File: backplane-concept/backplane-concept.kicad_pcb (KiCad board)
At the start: 2 copper layers, 90 x 150 mm, 55 parts, among them J1 6473427-1, J2 PCIE_8x_Labeled, J3 PCIE_8x_Labeled, J4 PCIE_8x_Labeled, J5 CONN_MINI, J6 CONN_MINI, J7 CONN_MINI, J8 CONN_MINI, U1 PRIMARY, U2 SECONDARY, U3 NAU7802SGI, U4 ATA6561-GBQW-N, U5 ESP32-PICO-D4, U6 5V Reg, U7 AMS1117CD-5.0, U8 3.3V Reg, U9 AMS1117CD-3.3

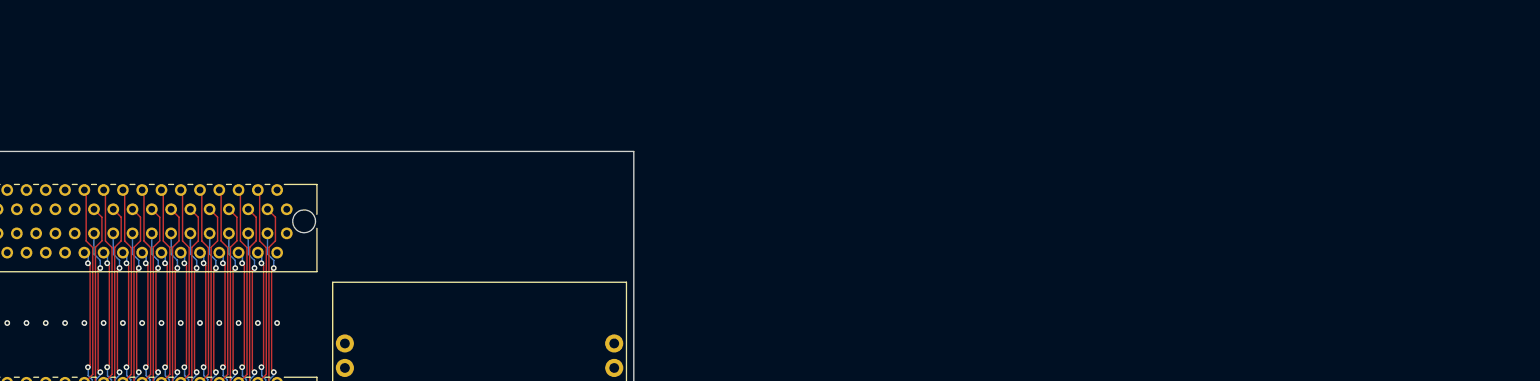
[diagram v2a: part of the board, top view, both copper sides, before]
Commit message: Add testpoints
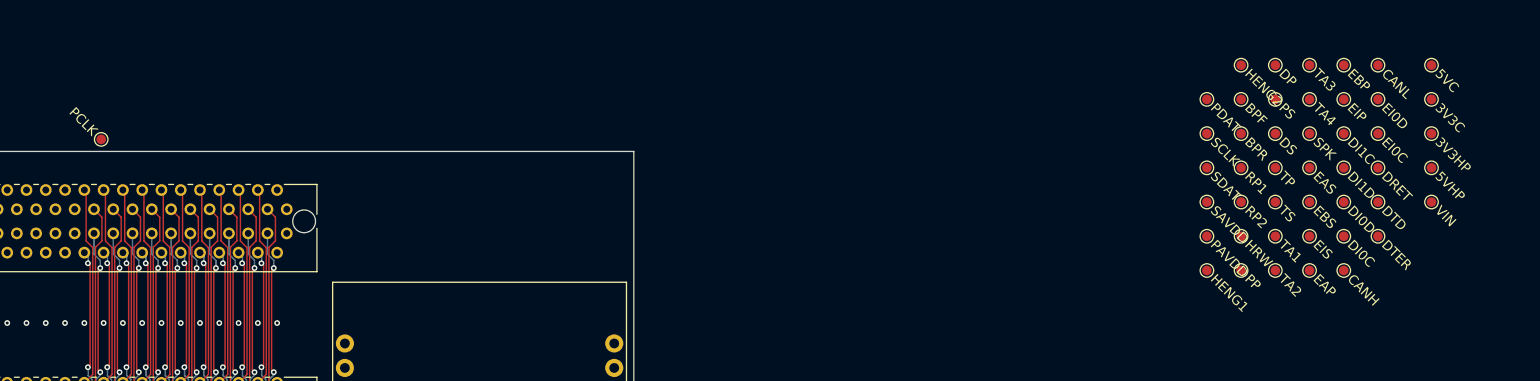
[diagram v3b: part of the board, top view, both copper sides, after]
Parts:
- added TP1: PCLK, !footprints:TestPoint_Pad_D1.0mm, F.Cu at (90.8, 32.8)
- added TP10: 5VHP, !footprints:TestPoint_Pad_D1.0mm, F.Cu at (228.8, 35.7)
- added TP11: VIN, !footprints:TestPoint_Pad_D1.0mm, F.Cu at (228.8, 39.2)
- added TP12: HENG1, !footprints:TestPoint_Pad_D1.0mm, F.Cu at (205.4, 46.4)
- added TP13: HENG2, !footprints:TestPoint_Pad_D1.0mm, F.Cu at (209.0, 25.1)
- added TP14: BPF, !footprints:TestPoint_Pad_D1.0mm, F.Cu at (209.0, 28.6)
- added TP15: BPR, !footprints:TestPoint_Pad_D1.0mm, F.Cu at (209.0, 32.1)
- added TP16: RP1, !footprints:TestPoint_Pad_D1.0mm, F.Cu at (209.0, 35.7)
- added TP17: RP2, !footprints:TestPoint_Pad_D1.0mm, F.Cu at (209.0, 39.2)
- added TP18: HRW, !footprints:TestPoint_Pad_D1.0mm, F.Cu at (209.0, 42.8)
- added TP19: PP, !footprints:TestPoint_Pad_D1.0mm, F.Cu at (209.0, 46.4)
- added TP2: PDAT, !footprints:TestPoint_Pad_D1.0mm, F.Cu at (205.4, 28.6)
- added TP20: DP, !footprints:TestPoint_Pad_D1.0mm, F.Cu at (212.6, 25.1)
- added TP21: PS, !footprints:TestPoint_Pad_D1.0mm, F.Cu at (212.6, 28.6)
- added TP22: DS, !footprints:TestPoint_Pad_D1.0mm, F.Cu at (212.6, 32.1)
- added TP23: TP, !footprints:TestPoint_Pad_D1.0mm, F.Cu at (212.6, 35.7)
- added TP24: TS, !footprints:TestPoint_Pad_D1.0mm, F.Cu at (212.6, 39.2)
- added TP25: TA1, !footprints:TestPoint_Pad_D1.0mm, F.Cu at (212.6, 42.8)
- added TP26: TA2, !footprints:TestPoint_Pad_D1.0mm, F.Cu at (212.6, 46.4)
- added TP27: TA3, !footprints:TestPoint_Pad_D1.0mm, F.Cu at (216.1, 25.1)
- added TP28: TA4, !footprints:TestPoint_Pad_D1.0mm, F.Cu at (216.1, 28.6)
- added TP29: SPK, !footprints:TestPoint_Pad_D1.0mm, F.Cu at (216.1, 32.1)
- added TP3: SCLK, !footprints:TestPoint_Pad_D1.0mm, F.Cu at (205.4, 32.1)
- added TP30: EAS, !footprints:TestPoint_Pad_D1.0mm, F.Cu at (216.1, 35.7)
- added TP31: EBS, !footprints:TestPoint_Pad_D1.0mm, F.Cu at (216.1, 39.2)
- added TP32: EIS, !footprints:TestPoint_Pad_D1.0mm, F.Cu at (216.1, 42.8)
- added TP33: EAP, !footprints:TestPoint_Pad_D1.0mm, F.Cu at (216.1, 46.4)
- added TP34: EBP, !footprints:TestPoint_Pad_D1.0mm, F.Cu at (219.7, 25.1)
- added TP35: EIP, !footprints:TestPoint_Pad_D1.0mm, F.Cu at (219.7, 28.6)
- added TP36: DI1C, !footprints:TestPoint_Pad_D1.0mm, F.Cu at (219.7, 32.1)
- added TP37: DI1D, !footprints:TestPoint_Pad_D1.0mm, F.Cu at (219.7, 35.7)
- added TP38: DI0D, !footprints:TestPoint_Pad_D1.0mm, F.Cu at (219.7, 39.2)
- added TP39: DI0C, !footprints:TestPoint_Pad_D1.0mm, F.Cu at (219.7, 42.8)
- added TP4: SDAT, !footprints:TestPoint_Pad_D1.0mm, F.Cu at (205.4, 35.7)
- added TP40: CANH, !footprints:TestPoint_Pad_D1.0mm, F.Cu at (219.7, 46.4)
- added TP41: CANL, !footprints:TestPoint_Pad_D1.0mm, F.Cu at (223.2, 25.1)
- added TP42: EI0D, !footprints:TestPoint_Pad_D1.0mm, F.Cu at (223.2, 28.6)
- added TP43: EI0C, !footprints:TestPoint_Pad_D1.0mm, F.Cu at (223.2, 32.1)
- added TP44: DRET, !footprints:TestPoint_Pad_D1.0mm, F.Cu at (223.2, 35.7)
- added TP45: DTD, !footprints:TestPoint_Pad_D1.0mm, F.Cu at (223.2, 39.2)
- added TP46: DTER, !footprints:TestPoint_Pad_D1.0mm, F.Cu at (223.2, 42.8)
- added TP5: SAVDD, !footprints:TestPoint_Pad_D1.0mm, F.Cu at (205.4, 39.2)
- added TP6: PAVDD, !footprints:TestPoint_Pad_D1.0mm, F.Cu at (205.4, 42.8)
- added TP7: 5VC, !footprints:TestPoint_Pad_D1.0mm, F.Cu at (228.8, 25.1)
- added TP8: 3V3C, !footprints:TestPoint_Pad_D1.0mm, F.Cu at (228.8, 28.6)
- added TP9: 3V3HP, !footprints:TestPoint_Pad_D1.0mm, F.Cu at (228.8, 32.1)
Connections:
- net AVDD_S renamed AVDD_P
- C10 pad 1: +3.3VA -> /PSU/3V3_CLEAN
- C12 pad 1: +8V -> /PSU/VIN
- C14 pad 1: +5V -> /PSU/5V_HP
- C15 pad 1: +5V -> /PSU/5V_HP
- C18 pad 1: +8V -> /PSU/VIN
- C23 pad 1: +3V3 -> /PSU/3V3_HP
- C24 pad 1: +3V3 -> /PSU/3V3_HP
- C25 pad 1: +8V -> /PSU/VIN
- C26 pad 1: +8V -> /PSU/VIN
- C7 pad 1: +8V -> /PSU/VIN
- C8 pad 1: +5VA -> /PSU/5V_CLEAN
- C9 pad 1: +8V -> /PSU/VIN
- L1 pad 2: +5V -> /PSU/5V_HP
- L2 pad 2: +3V3 -> /PSU/3V3_HP
- R6 pad 1: +5V -> /PSU/5V_HP
- R9 pad 1: +3V3 -> /PSU/3V3_HP
- U2 pad 7: LOADC_CLK_P -> LOADC_CLK_S
- U6 pad 2: +8V -> /PSU/VIN
- U6 pad 3: +8V -> /PSU/VIN
- U7 pad 2: +5VA -> /PSU/5V_CLEAN
- U7 pad 3: +8V -> /PSU/VIN
- U8 pad 2: +8V -> /PSU/VIN
- U8 pad 3: +8V -> /PSU/VIN
- U9 pad 2: +3.3VA -> /PSU/3V3_CLEAN
- U9 pad 3: +8V -> /PSU/VIN
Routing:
- net /PSU/VIN: vias 0 -> 4
- net +8V: vias 26 -> 22

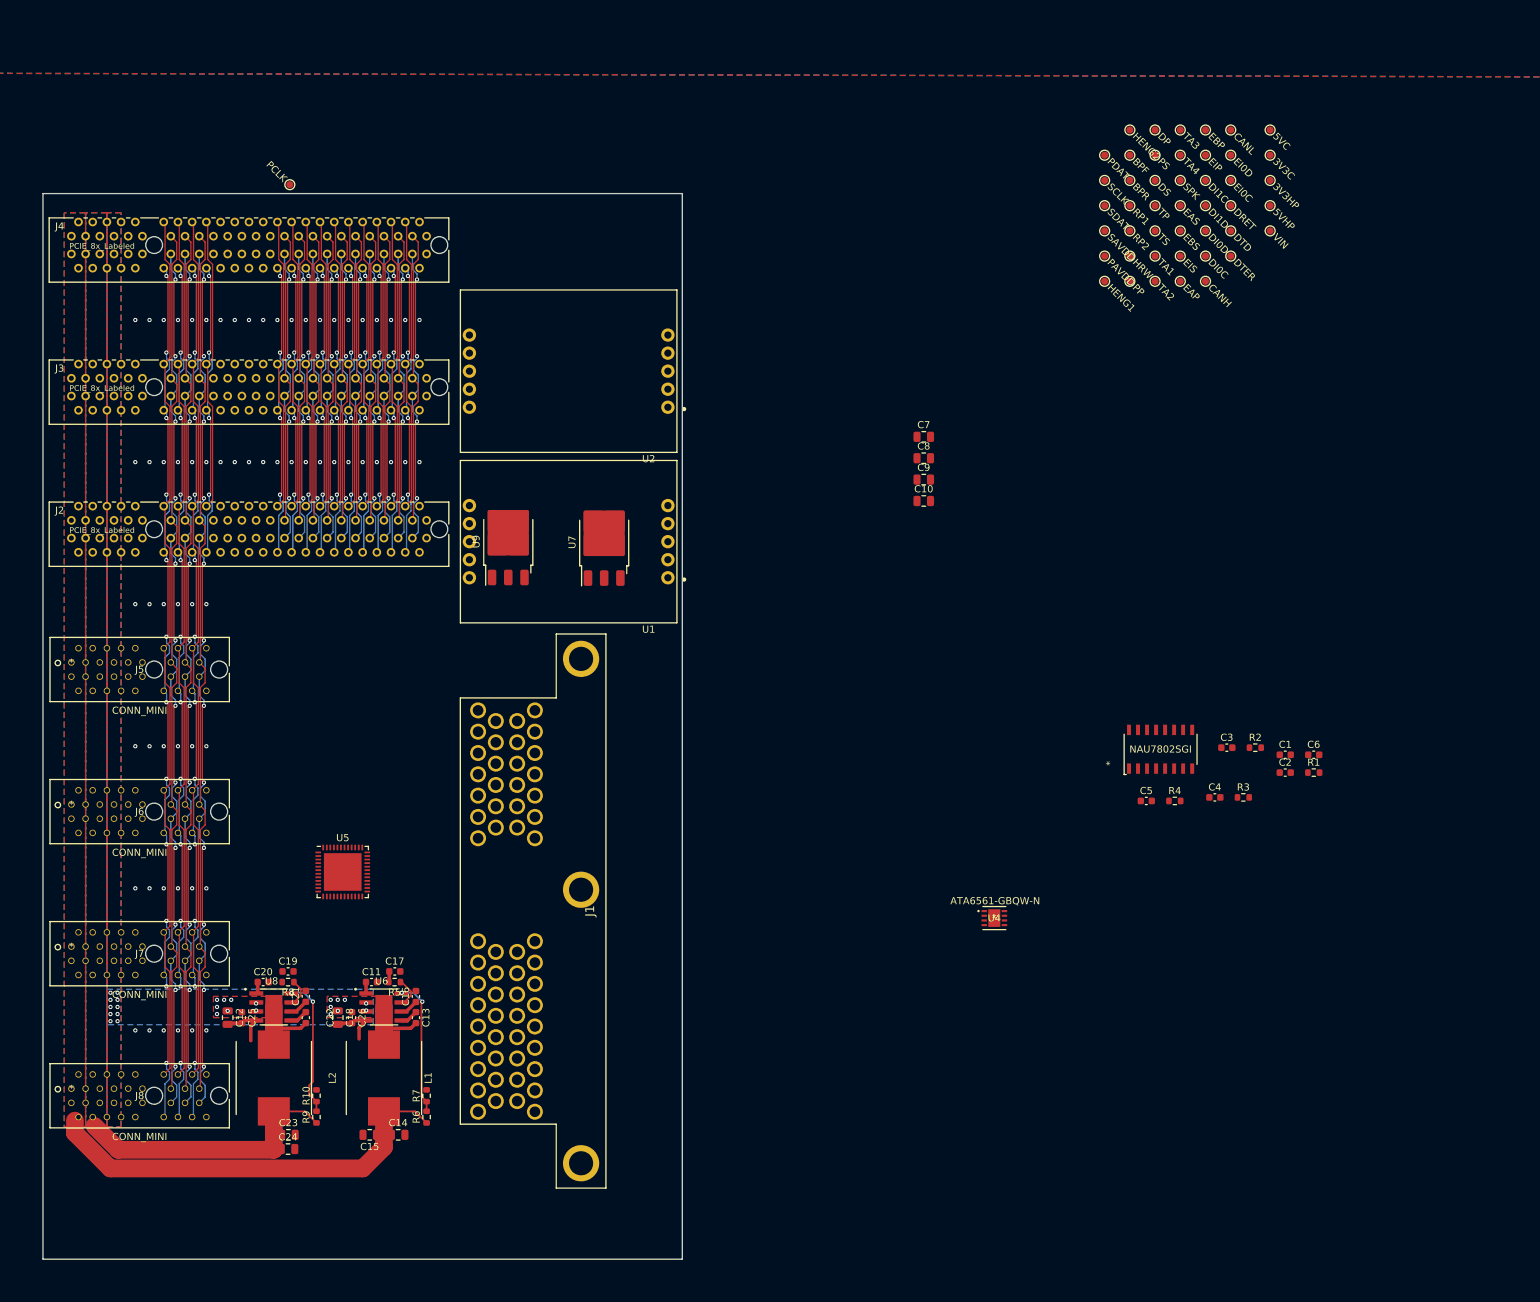
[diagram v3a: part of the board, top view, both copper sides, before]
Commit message: Route some test points
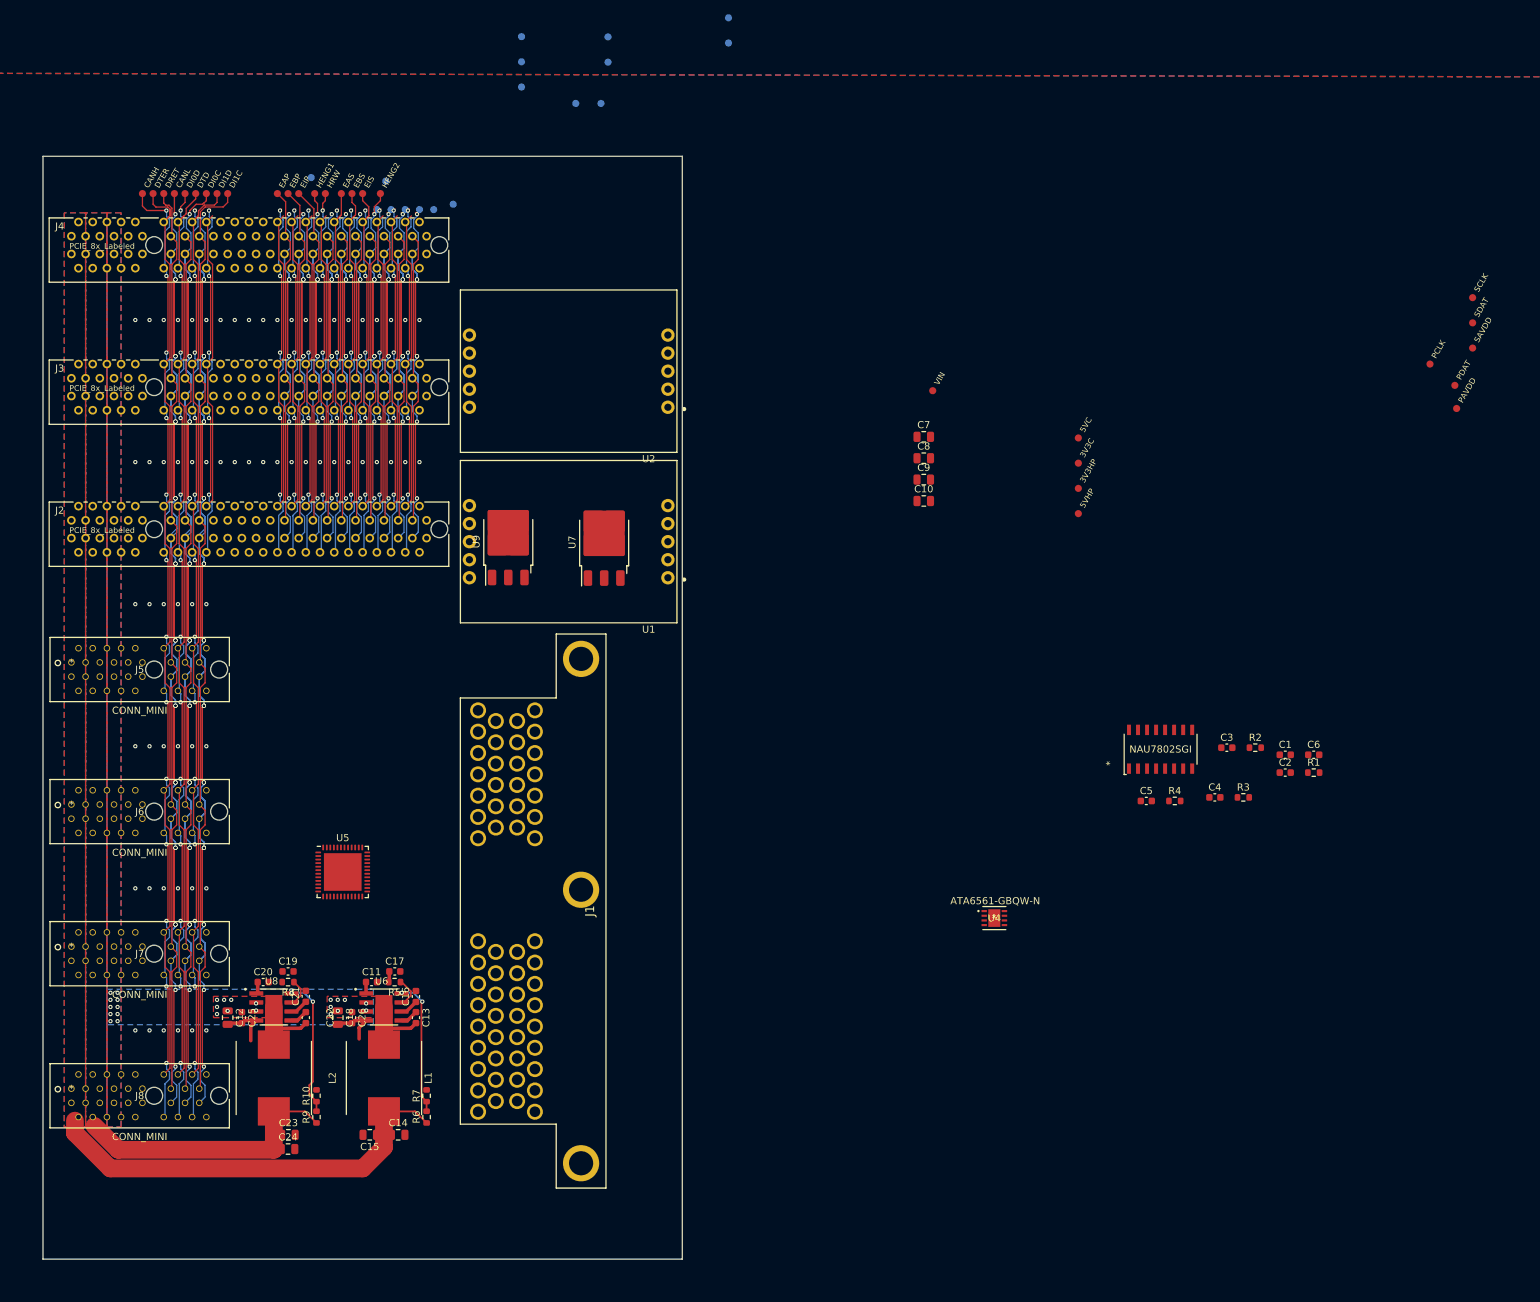
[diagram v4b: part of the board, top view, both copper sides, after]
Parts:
- TP14, TP15, TP16, TP17, TP19, TP20, TP21, TP22, TP23, TP24, TP25, TP26, TP27, TP28, TP29, TP42, TP43: moved to B.Cu
- moved TP1 162.5 mm to (251.2, 58.0), turned to 0 degrees
- moved TP46 152.0 mm to (71.5, 34.0)
- moved TP44 150.2 mm to (73.0, 34.0)
- moved TP40 150.2 mm to (70.0, 34.0)
- moved TP41 149.0 mm to (74.5, 34.0)
- moved TP45 145.8 mm to (77.5, 34.0)
- moved TP38 143.7 mm to (76.0, 34.0)
- moved TP39 140.9 mm to (79.0, 34.0)
- moved TP37 139.2 mm to (80.5, 34.0)
- moved TP36 137.7 mm to (82.0, 34.0)
- moved TP34 129.5 mm to (90.5, 34.0)
- moved TP35 127.8 mm to (92.0, 34.0)
- moved TP33 127.7 mm to (89.0, 34.0)
- moved TP30 118.1 mm to (98.0, 34.0)
- moved TP31 116.7 mm to (99.5, 34.0)
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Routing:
- net I2C0_DAQ_SCL: track 127.0 -> 243.9 mm, vias 12 -> 23
- net CAN_L: track 127.0 -> 242.5 mm, vias 12 -> 23
- net I2C0_ECVT_SCL: track 127.0 -> 239.5 mm, vias 12 -> 23
- net GND: track 467.0 -> 523.6 mm, vias 82 -> 88
- net HALL_ENG2: track 42.5 -> 73.7 mm, vias 4 -> 7
- net HALL_ENG1: track 42.5 -> 73.5 mm, vias 4 -> 7
- net BP_REAR: track 42.5 -> 70.5 mm, vias 4 -> 7
- net RPOT2: track 42.5 -> 70.5 mm, vias 4 -> 7
- net PWM_S: track 42.5 -> 70.5 mm, vias 4 -> 7
- net LOADC_DAT_P: track 42.5 -> 70.5 mm, vias 4 -> 7
- net I2C1_ECVT_EXT_SDA: track 42.5 -> 70.5 mm, vias 4 -> 7
- net PWM_P: track 42.5 -> 70.5 mm, vias 4 -> 7
- net LOADC_DAT_S: track 42.5 -> 70.5 mm, vias 4 -> 7
- net LOADC_CLK_P: track 82.5 -> 99.9 mm, vias 8 -> 10
- net CAN_H: track 123.8 -> 137.6 mm, vias 12 -> 13
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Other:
- board size 90 x 150 mm -> 90 x 155.2 mm

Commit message: More routing
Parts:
- added TP42: EI0D, !footprints:TestPoint_Pad_D1.0mm, B.Cu at (153.0, 29.0)
- added TP42: EI0D, !footprints:TestPoint_Pad_D1.0mm, B.Cu at (150.5, 25.0)
- added TP42: EI0D, !footprints:TestPoint_Pad_D1.0mm, B.Cu at (150.5, 21.8)
- added TP42: EI0D, !footprints:TestPoint_Pad_D1.0mm, B.Cu at (150.2, 29.0)
- added TP42: EI0D, !footprints:TestPoint_Pad_D1.0mm, B.Cu at (153.2, 25.0)
- TP42: moved to F.Cu
- moved TP9 141.8 mm to (94.5, 168.2)
- moved TP10 136.6 mm to (98.2, 168.2)
- moved TP22 25.4 mm to (99.5, 27.8), turned to 120 degrees
- moved TP42 19.2 mm to (153.8, 21.8), turned to 60 degrees
- moved TP19 4.93 mm to (96.2, 27.5), turned to 120 degrees
- moved TP24 4.81 mm to (107.2, 34.0), turned to 120 degrees
- moved TP15 3.96 mm to (149.7, 10.0), turned to 120 degrees
- moved TP20 3.96 mm to (126.2, 14.7), turned to 120 degrees
- moved TP17 3.95 mm to (132.7, 12.8), turned to 120 degrees
- moved TP25 2.85 mm to (108.8, 34.0), turned to 120 degrees
- moved TP26 2.57 mm to (110.2, 34.0), turned to 120 degrees
- moved TP23 2.37 mm to (105.8, 34.0), turned to 120 degrees
- moved TP27 2.37 mm to (111.8, 34.0), turned to 120 degrees
- moved TP29 1.90 mm to (103.5, 34.0), turned to 120 degrees
- moved TP28 1.58 mm to (113.2, 34.0), turned to 120 degrees
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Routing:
- net /PSU/5V_HP: track 0.00 -> 5.29 mm
- net /PSU/3V3_HP: track 0.00 -> 3.29 mm
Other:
- board text added: "Single Flip"
- board text added: "Single Rotation"
- board text added: "Single Rotation (Center-Aligned)"
